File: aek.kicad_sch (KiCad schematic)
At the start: 242 parts, among them J1 Conn_01x04_MountingPin, SW1 SW_Push, U1 ATmega32U4-AU, U2 ATmega32U4-AU, Y1 16MHz

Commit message: updates
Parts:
- U2: value ATmega32U4-AU -> ATmega32U4-MU
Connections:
- net ROW1: now also U1.11 (PB3), U2.11 (PB3); no longer U1.18 (PD0), U2.18 (PD0)
- net ROW10: now also U1.9 (PB1), U2.9 (PB1); no longer U1.20 (PD2), U2.20 (PD2)
- net ROW2: now also U1.12 (PB7), U2.12 (PB7); no longer U1.9 (PB1), U2.9 (PB1)
- net ROW3: now also U1.19 (PD1), U2.19 (PD1); no longer U1.11 (PB3), U2.11 (PB3)
- net ROW7: now also U1.20 (PD2), U2.20 (PD2); no longer U1.12 (PB7), U2.12 (PB7)
- net ROW8: now also U1.18 (PD0), U2.18 (PD0); no longer U1.10 (PB2), U2.10 (PB2)
- net ROW9: now also U1.10 (PB2), U2.10 (PB2); no longer U1.19 (PD1), U2.19 (PD1)
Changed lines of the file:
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@@
     )
   )
-  (global_label "ROW2" (shape input) (at 87.63 62.23 0) (fields_autoplaced)
+  (global_label "ROW10" (shape input) (at 87.63 62.23 0) (fields_autoplaced)
     (effects (font (size 1.27 1.27)) (justify left))
-    (property "Intersheet References" "${INTERSHEET_REFS}" (id 0) (at 7.62 -41.91 0)
+    (property "Intersheet References" "${INTERSHEET_REFS}" (id 0) (at 7.62 -74.93 0)
       (effects (font (size 1.27 1.27)) hide)
     )
   )
-  (global_label "ROW8" (shape input) (at 87.63 64.77 0) (fields_autoplaced)
+  (global_label "ROW9" (shape input) (at 87.63 64.77 0) (fields_autoplaced)
     (effects (font (size 1.27 1.27)) (justify left))
-    (property "Intersheet References" "${INTERSHEET_REFS}" (id 0) (at 7.62 -41.91 0)
+    (property "Intersheet References" "${INTERSHEET_REFS}" (id 0) (at 7.62 -69.85 0)
       (effects (font (size 1.27 1.27)) hide)
     )
   )
-  (global_label "ROW3" (shape input) (at 87.63 67.31 0) (fields_autoplaced)
+  (global_label "ROW1" (shape input) (at 87.63 67.31 0) (fields_autoplaced)
     (effects (font (size 1.27 1.27)) (justify left))
-    (property "Intersheet References" "${INTERSHEET_REFS}" (id 0) (at 7.62 -41.91 0)
+    (property "Intersheet References" "${INTERSHEET_REFS}" (id 0) (at 7.62 -64.77 0)
       (effects (font (size 1.27 1.27)) hide)
     )
@@
     )
   )
-  (global_label "ROW7" (shape input) (at 87.63 77.47 0) (fields_autoplaced)
+  (global_label "ROW2" (shape input) (at 87.63 77.47 0) (fields_autoplaced)
     (effects (font (size 1.27 1.27)) (justify left))
-    (property "Intersheet References" "${INTERSHEET_REFS}" (id 0) (at 7.62 -41.91 0)
+    (property "Intersheet References" "${INTERSHEET_REFS}" (id 0) (at 7.62 -26.67 0)
       (effects (font (size 1.27 1.27)) hide)
     )
@@
     )
   )
-  (global_label "ROW1" (shape input) (at 87.63 90.17 0) (fields_autoplaced)
+  (global_label "ROW8" (shape input) (at 87.63 90.17 0) (fields_autoplaced)
     (effects (font (size 1.27 1.27)) (justify left))
-    (property "Intersheet References" "${INTERSHEET_REFS}" (id 0) (at 7.62 -41.91 0)
+    (property "Intersheet References" "${INTERSHEET_REFS}" (id 0) (at 7.62 -16.51 0)
       (effects (font (size 1.27 1.27)) hide)
     )
   )
-  (global_label "ROW9" (shape input) (at 87.63 92.71 0) (fields_autoplaced)
+  (global_label "ROW3" (shape input) (at 87.63 92.71 0) (fields_autoplaced)
     (effects (font (size 1.27 1.27)) (justify left))
-    (property "Intersheet References" "${INTERSHEET_REFS}" (id 0) (at 7.62 -41.91 0)
+    (property "Intersheet References" "${INTERSHEET_REFS}" (id 0) (at 7.62 -16.51 0)
       (effects (font (size 1.27 1.27)) hide)
     )
   )
-  (global_label "ROW10" (shape input) (at 87.63 95.25 0) (fields_autoplaced)
+  (global_label "ROW7" (shape input) (at 87.63 95.25 0) (fields_autoplaced)
     (effects (font (size 1.27 1.27)) (justify left))
-    (property "Intersheet References" "${INTERSHEET_REFS}" (id 0) (at 7.62 -41.91 0)
+    (property "Intersheet References" "${INTERSHEET_REFS}" (id 0) (at 7.62 -24.13 0)
       (effects (font (size 1.27 1.27)) hide)
     )
@@
     (in_bom yes) (on_board yes)
     (property "Reference" "U2" (id 0) (at 72.39 145.7706 0))
-    (property "Value" "ATmega32U4-AU" (id 1) (at 72.39 148.082 0))
+    (property "Value" "ATmega32U4-MU" (id 1) (at 72.39 148.082 0))
     (property "Footprint" "Package_DFN_QFN:QFN-44-1EP_7x7mm_P0.5mm_EP5.2x5.2mm" (id 2) (at 72.39 97.79 0)
       (effects (font (size 1.27 1.27) italic) hide)
@@
     )
     (path "/2ccdb65d-62ed-42d5-acea-df4cedf22149"
-      (reference "U2") (unit 1) (value "ATmega32U4-AU") (footprint "Package_DFN_QFN:QFN-44-1EP_7x7mm_P0.5mm_EP5.2x5.2mm")
+      (reference "U2") (unit 1) (value "ATmega32U4-MU") (footprint "Package_DFN_QFN:QFN-44-1EP_7x7mm_P0.5mm_EP5.2x5.2mm")
     )
     (path "/00000000-0000-0000-0000-0000612269b2"

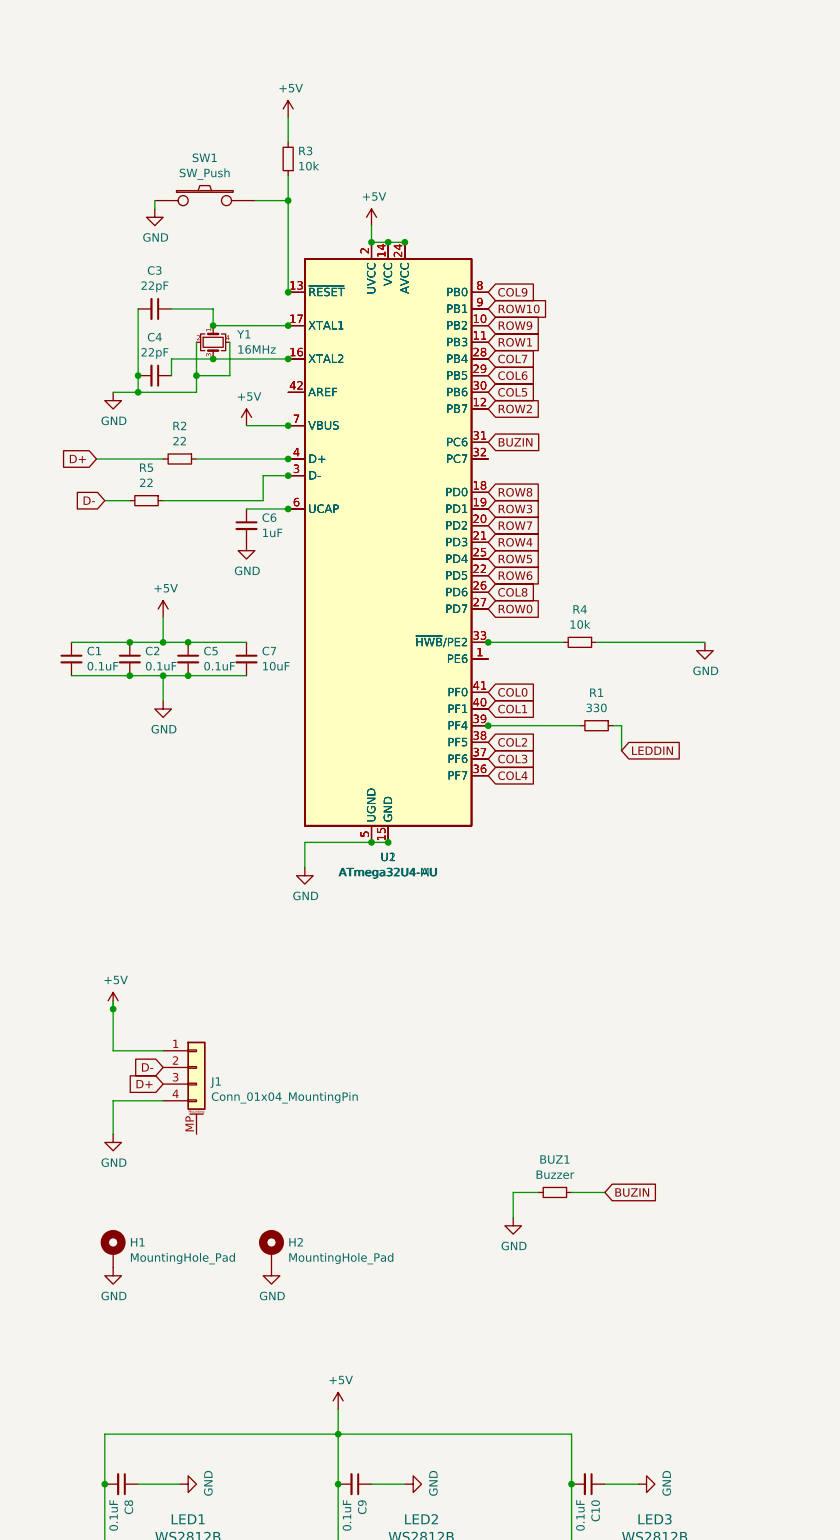
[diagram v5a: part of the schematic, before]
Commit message: continuous ground on F.Cu and custom footprint for merged au/mu atmega32u4
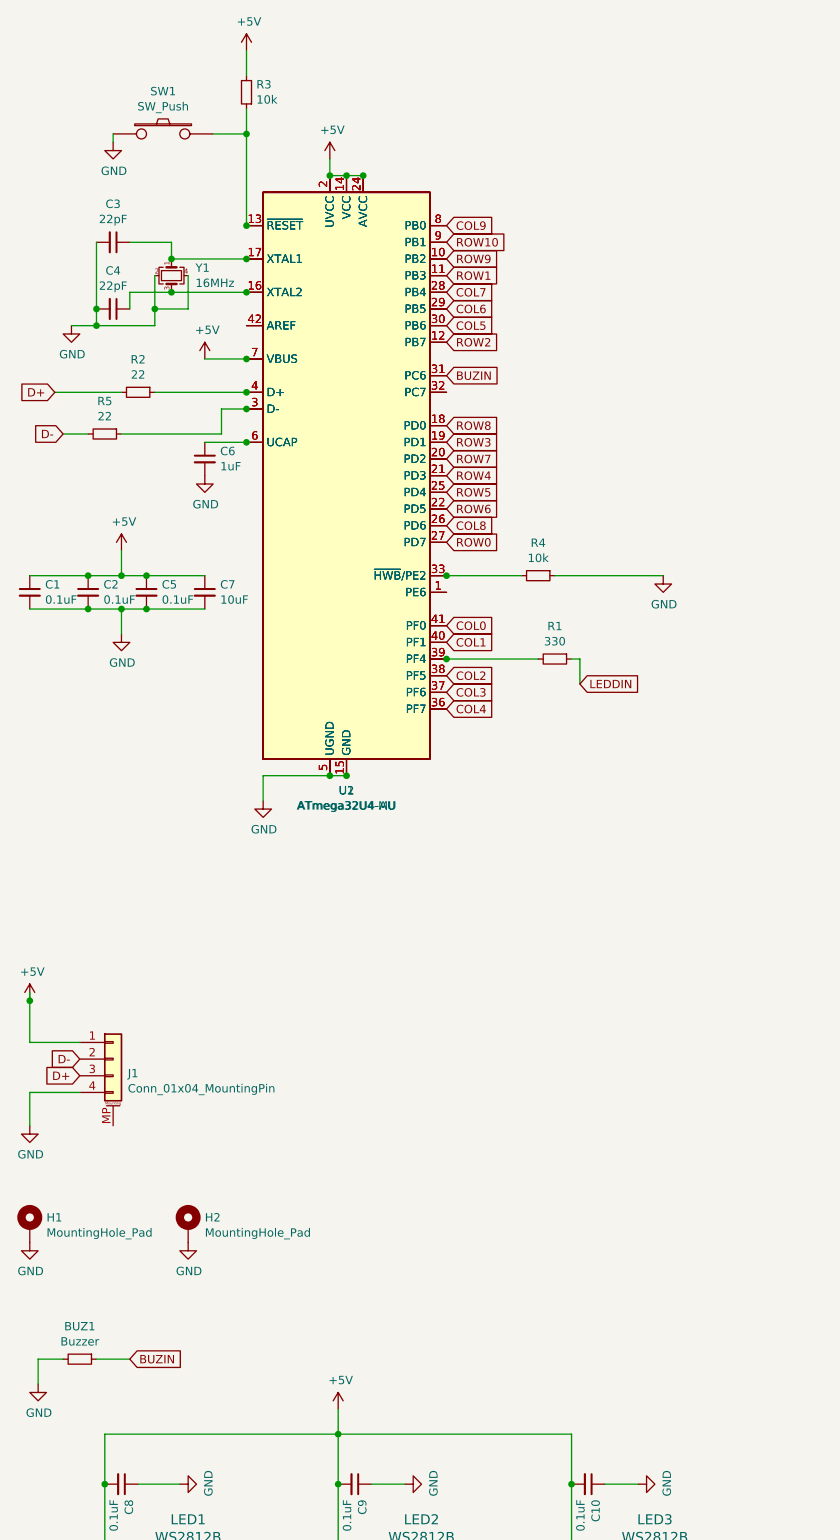
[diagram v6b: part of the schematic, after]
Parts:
- U2: symbol MCU_Microchip_ATmega:ATmega32U4-AU -> MCU_Microchip_ATmega:ATmega32U4-MU
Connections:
- net GND: now also U2.45 (GND)
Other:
- moved on the sheet: BUZ1, C1, C2, C3, C4, C5, C6, C7, H1, H2, J1, R1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

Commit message: cleanup
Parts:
- removed U1: ATmega32U4-AU, Package_QFP:TQFP-44_10x10mm_P0.8mm, symbol MCU_Microchip_ATmega:ATmega32U4-AU
- U1: renamed from U2; footprint Package_DFN_QFN:QFN-44-1EP_7x7mm_P0.5mm_EP5.2x5.2mm -> atmega32u4-au-and-mu:atmega32u4-mu-and-au
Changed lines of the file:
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@@
   (junction (at 39.37 59.69) (diameter 1.016) (color 0 0 0 0))
   (junction (at 50.8 35.56) (diameter 1.016) (color 0 0 0 0))
-  (junction (at 50.8 49.53) (diameter 1.016) (color 0 0 0 0))
-  (junction (at 50.8 54.61) (diameter 1.016) (color 0 0 0 0))
-  (junction (at 50.8 59.69) (diameter 1.016) (color 0 0 0 0))
-  (junction (at 50.8 69.85) (diameter 1.016) (color 0 0 0 0))
-  (junction (at 50.8 74.93) (diameter 1.016) (color 0 0 0 0))
-  (junction (at 50.8 77.47) (diameter 1.016) (color 0 0 0 0))
-  (junction (at 50.8 82.55) (diameter 1.016) (color 0 0 0 0))
   (junction (at 63.5 41.91) (diameter 1.016) (color 0 0 0 0))
   (junction (at 63.5 133.35) (diameter 1.016) (color 0 0 0 0))
@@
   (junction (at 64.77 241.3) (diameter 1.016) (color 0 0 0 0))
   (junction (at 66.04 41.91) (diameter 1.016) (color 0 0 0 0))
-  (junction (at 66.04 133.35) (diameter 1.016) (color 0 0 0 0))
-  (junction (at 68.58 41.91) (diameter 1.016) (color 0 0 0 0))
-  (junction (at 81.28 102.87) (diameter 1.016) (color 0 0 0 0))
-  (junction (at 81.28 115.57) (diameter 1.016) (color 0 0 0 0))
   (junction (at 100.33 241.3) (diameter 1.016) (color 0 0 0 0))
   (junction (at 157.48 55.88) (diameter 1.016) (color 0 0 0 0))
@@
     (pin "4")
   )
-  (symbol (lib_id "MCU_Microchip_ATmega:ATmega32U4-AU") (at 66.04 87.63 0) (unit 1)
-    (in_bom yes) (on_board yes)
-    (property "Reference" "U1" (id 0) (at 66.04 135.6106 0))
-    (property "Value" "ATmega32U4-AU" (id 1) (at 66.04 137.922 0))
-    (property "Footprint" "Package_QFP:TQFP-44_10x10mm_P0.8mm" (id 2) (at 66.04 87.63 0)
-      (effects (font (size 1.27 1.27) italic) hide)
-    )
-    (property "Datasheet" "http://ww1.microchip.com/downloads/en/DeviceDoc/Atmel-7766-8-bit-AVR-ATmega16U4-32U4_Datasheet.pdf" (id 3) (at 66.04 87.63 0)
-      (effects (font (size 1.27 1.27)) hide)
-    )
-    (pin "1")
-    (pin "10")
-    (pin "11")
-    (pin "12")
-    (pin "13")
-    (pin "14")
-    (pin "15")
-    (pin "16")
-    (pin "17")
-    (pin "18")
-    (pin "19")
-    (pin "2")
-    (pin "20")
-    (pin "21")
-    (pin "22")
-    (pin "23")
-    (pin "24")
-    (pin "25")
-    (pin "26")
-    (pin "27")
-    (pin "28")
-    (pin "29")
-    (pin "3")
-    (pin "30")
-    (pin "31")
-    (pin "32")
-    (pin "33")
-    (pin "34")
-    (pin "35")
-    (pin "36")
-    (pin "37")
-    (pin "38")
-    (pin "39")
-    (pin "4")
-    (pin "40")
-    (pin "41")
-    (pin "42")
-    (pin "43")
-    (pin "44")
-    (pin "5")
-    (pin "6")
-    (pin "7")
-    (pin "8")
-    (pin "9")
-  )
   (symbol (lib_id "MCU_Microchip_ATmega:ATmega32U4-MU") (at 66.04 87.63 0) (unit 1)
     (in_bom yes) (on_board yes)
-    (property "Reference" "U2" (id 0) (at 66.04 135.6106 0))
+    (property "Reference" "U1" (id 0) (at 66.04 135.6106 0))
     (property "Value" "ATmega32U4-MU" (id 1) (at 66.04 137.922 0))
-    (property "Footprint" "Package_DFN_QFN:QFN-44-1EP_7x7mm_P0.5mm_EP5.2x5.2mm" (id 2) (at 66.04 87.63 0)
+    (property "Footprint" "atmega32u4-au-and-mu:atmega32u4-mu-and-au" (id 2) (at 66.04 87.63 0)
       (effects (font (size 1.27 1.27) italic) hide)
     )
@@
       (reference "SW_Z1") (unit 1) (value "MX-NoLED") (footprint "MX_Alps_Hybrid:MX-1U-NoLED")
     )
-    (path "/00000000-0000-0000-0000-0000611ebb71"
-      (reference "U1") (unit 1) (value "ATmega32U4-AU") (footprint "Package_QFP:TQFP-44_10x10mm_P0.8mm")
-    )
     (path "/2ccdb65d-62ed-42d5-acea-df4cedf22149"
-      (reference "U2") (unit 1) (value "ATmega32U4-MU") (footprint "Package_DFN_QFN:QFN-44-1EP_7x7mm_P0.5mm_EP5.2x5.2mm")
+      (reference "U1") (unit 1) (value "ATmega32U4-MU") (footprint "atmega32u4-au-and-mu:atmega32u4-mu-and-au")
     )
     (path "/00000000-0000-0000-0000-0000612269b2"

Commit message: bug fixes
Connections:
- net +5V: now also J1.4 (Pin_4); no longer J1.1 (Pin_1)
- net D+: now also J1.2 (Pin_2); no longer J1.3 (Pin_3)
- net D-: now also J1.3 (Pin_3); no longer J1.2 (Pin_2)
- net GND: now also J1.1 (Pin_1); no longer J1.4 (Pin_4)
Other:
- moved on the sheet: J1
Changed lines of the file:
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@@
 (kicad_sch (version 20210621) (generator eeschema)
   (paper "User" 359.994 359.994)
-  (junction (at 17.78 167.64) (diameter 1.016) (color 0 0 0 0))
   (junction (at 26.67 102.87) (diameter 1.016) (color 0 0 0 0))
   (junction (at 26.67 107.95) (diameter 1.016) (color 0 0 0 0))
@@
   (junction (at 39.37 59.69) (diameter 1.016) (color 0 0 0 0))
   (junction (at 50.8 35.56) (diameter 1.016) (color 0 0 0 0))
+  (junction (at 53.34 170.18) (diameter 1.016) (color 0 0 0 0))
   (junction (at 63.5 41.91) (diameter 1.016) (color 0 0 0 0))
   (junction (at 63.5 133.35) (diameter 1.016) (color 0 0 0 0))
@@
     (stroke (width 0) (type solid) (color 0 0 0 0))
   )
-  (wire (pts (xy 17.78 166.37) (xy 17.78 167.64))
-    (stroke (width 0) (type solid) (color 0 0 0 0))
-  )
-  (wire (pts (xy 17.78 167.64) (xy 17.78 173.99))
-    (stroke (width 0) (type solid) (color 0 0 0 0))
-  )
-  (wire (pts (xy 17.78 181.61) (xy 17.78 186.69))
-    (stroke (width 0) (type solid) (color 0 0 0 0))
-  )
   (wire (pts (xy 19.05 222.25) (xy 19.05 226.06))
     (stroke (width 0) (type solid) (color 0 0 0 0))
@@
     (stroke (width 0) (type solid) (color 0 0 0 0))
   )
-  (wire (pts (xy 25.4 173.99) (xy 17.78 173.99))
-    (stroke (width 0) (type solid) (color 0 0 0 0))
-  )
-  (wire (pts (xy 25.4 181.61) (xy 17.78 181.61))
-    (stroke (width 0) (type solid) (color 0 0 0 0))
-  )
   (wire (pts (xy 26.67 102.87) (xy 31.75 102.87))
     (stroke (width 0) (type solid) (color 0 0 0 0))
@@
     (stroke (width 0) (type solid) (color 0 0 0 0))
   )
+  (wire (pts (xy 45.72 175.26) (xy 53.34 175.26))
+    (stroke (width 0) (type solid) (color 0 0 0 0))
+  )
   (wire (pts (xy 46.99 77.47) (xy 50.8 77.47))
     (stroke (width 0) (type solid) (color 0 0 0 0))
@@
     (stroke (width 0) (type solid) (color 0 0 0 0))
   )
+  (wire (pts (xy 53.34 168.91) (xy 53.34 170.18))
+    (stroke (width 0) (type solid) (color 0 0 0 0))
+  )
+  (wire (pts (xy 53.34 170.18) (xy 53.34 175.26))
+    (stroke (width 0) (type solid) (color 0 0 0 0))
+  )
+  (wire (pts (xy 53.34 182.88) (xy 45.72 182.88))
+    (stroke (width 0) (type solid) (color 0 0 0 0))
+  )
+  (wire (pts (xy 53.34 182.88) (xy 53.34 189.23))
+    (stroke (width 0) (type solid) (color 0 0 0 0))
+  )
   (wire (pts (xy 54.61 259.08) (xy 54.61 254))
     (stroke (width 0) (type solid) (color 0 0 0 0))
@@
     )
   )
-  (global_label "D-" (shape input) (at 25.4 176.53 180) (fields_autoplaced)
-    (effects (font (size 1.27 1.27)) (justify right))
-    (property "Intersheet References" "${INTERSHEET_REFS}" (id 0) (at -12.7 -40.64 0)
-      (effects (font (size 1.27 1.27)) hide)
+  (global_label "BUZIN" (shape input) (at 33.02 222.25 0) (fields_autoplaced)
+    (effects (font (size 1.27 1.27)) (justify left))
+    (property "Intersheet References" "${INTERSHEET_REFS}" (id 0) (at 41.0386 222.1706 0)
+      (effects (font (size 1.27 1.27)) (justify left) hide)
     )
   )
-  (global_label "D+" (shape input) (at 25.4 179.07 180) (fields_autoplaced)
-    (effects (font (size 1.27 1.27)) (justify right))
-    (property "Intersheet References" "${INTERSHEET_REFS}" (id 0) (at -12.7 -40.64 0)
+  (global_label "D-" (shape input) (at 45.72 177.8 0) (fields_autoplaced)
+    (effects (font (size 1.27 1.27)) (justify left))
+    (property "Intersheet References" "${INTERSHEET_REFS}" (id 0) (at 83.82 394.97 0)
       (effects (font (size 1.27 1.27)) hide)
     )
   )
-  (global_label "BUZIN" (shape input) (at 33.02 222.25 0) (fields_autoplaced)
+  (global_label "D+" (shape input) (at 45.72 180.34 0) (fields_autoplaced)
     (effects (font (size 1.27 1.27)) (justify left))
-    (property "Intersheet References" "${INTERSHEET_REFS}" (id 0) (at 41.0386 222.1706 0)
-      (effects (font (size 1.27 1.27)) (justify left) hide)
+    (property "Intersheet References" "${INTERSHEET_REFS}" (id 0) (at 83.82 400.05 0)
+      (effects (font (size 1.27 1.27)) hide)
     )
   )
@@
     )
   )
-  (symbol (lib_id "power:+5V") (at 17.78 167.64 0) (unit 1)
-    (in_bom yes) (on_board yes)
-    (property "Reference" "#PWR0111" (id 0) (at 17.78 171.45 0)
-      (effects (font (size 1.27 1.27)) hide)
-    )
-    (property "Value" "+5V" (id 1) (at 18.161 163.2458 0))
-    (property "Footprint" "" (id 2) (at 17.78 167.64 0)
-      (effects (font (size 1.27 1.27)) hide)
-    )
-    (property "Datasheet" "" (id 3) (at 17.78 167.64 0)
-      (effects (font (size 1.27 1.27)) hide)
-    )
-    (pin "1")
-  )
   (symbol (lib_id "power:+5V") (at 31.75 99.06 0) (unit 1)
     (in_bom yes) (on_board yes)
@@
     (pin "1")
   )
+  (symbol (lib_id "power:+5V") (at 53.34 170.18 0) (unit 1)
+    (in_bom yes) (on_board yes)
+    (property "Reference" "#PWR0111" (id 0) (at 53.34 173.99 0)
+      (effects (font (size 1.27 1.27)) hide)
+    )
+    (property "Value" "+5V" (id 1) (at 53.721 165.7858 0))
+    (property "Footprint" "" (id 2) (at 53.34 170.18 0)
+      (effects (font (size 1.27 1.27)) hide)
+    )
+    (property "Datasheet" "" (id 3) (at 53.34 170.18 0)
+      (effects (font (size 1.27 1.27)) hide)
+    )
+    (pin "1")
+  )
   (symbol (lib_id "power:+5V") (at 63.5 39.37 0) (unit 1)
     (in_bom yes) (on_board yes)
@@
     (pin "1")
   )
-  (symbol (lib_id "power:GND") (at 17.78 186.69 0) (unit 1)
-    (in_bom yes) (on_board yes)
-    (property "Reference" "#PWR0112" (id 0) (at 17.78 193.04 0)
-      (effects (font (size 1.27 1.27)) hide)
-    )
-    (property "Value" "GND" (id 1) (at 17.907 191.0842 0))
-    (property "Footprint" "" (id 2) (at 17.78 186.69 0)
-      (effects (font (size 1.27 1.27)) hide)
-    )
-    (property "Datasheet" "" (id 3) (at 17.78 186.69 0)
-      (effects (font (size 1.27 1.27)) hide)
-    )
-    (pin "1")
-  )
   (symbol (lib_id "power:GND") (at 17.78 204.47 0) (unit 1)
     (in_bom yes) (on_board yes)
@@
     (pin "1")
   )
+  (symbol (lib_id "power:GND") (at 53.34 189.23 0) (unit 1)
+    (in_bom yes) (on_board yes)
+    (property "Reference" "#PWR0112" (id 0) (at 53.34 195.58 0)
+      (effects (font (size 1.27 1.27)) hide)
+    )
+    (property "Value" "GND" (id 1) (at 53.467 193.6242 0))
+    (property "Footprint" "" (id 2) (at 53.34 189.23 0)
+      (effects (font (size 1.27 1.27)) hide)
+    )
+    (property "Datasheet" "" (id 3) (at 53.34 189.23 0)
+      (effects (font (size 1.27 1.27)) hide)
+    )
+    (pin "1")
+  )
   (symbol (lib_id "power:GND") (at 54.61 270.51 0) (unit 1)
     (in_bom yes) (on_board yes)
@@
     (pin "2")
   )
-  (symbol (lib_id "Connector_Generic_MountingPin:Conn_01x04_MountingPin") (at 30.48 176.53 0) (unit 1)
+  (symbol (lib_id "Connector_Generic_MountingPin:Conn_01x04_MountingPin") (at 40.64 180.34 180) (unit 1)
     (in_bom yes) (on_board yes)
-    (property "Reference" "J1" (id 0) (at 32.7152 178.7144 0)
+    (property "Reference" "J1" (id 0) (at 38.4048 178.1556 0)
       (effects (font (size 1.27 1.27)) (justify left))
     )
-    (property "Value" "Conn_01x04_MountingPin" (id 1) (at 32.7152 181.0258 0)
+    (property "Value" "Conn_01x04_MountingPin" (id 1) (at 73.9648 178.3842 90)
       (effects (font (size 1.27 1.27)) (justify left))
     )
-    (property "Footprint" "Connector_JST:JST_SH_SM04B-SRSS-TB_1x04-1MP_P1.00mm_Horizontal" (id 2) (at 30.48 176.53 0)
+    (property "Footprint" "Connector_JST:JST_SH_SM04B-SRSS-TB_1x04-1MP_P1.00mm_Horizontal" (id 2) (at 40.64 180.34 0)
       (effects (font (size 1.27 1.27)) hide)
     )
-    (property "Datasheet" "~" (id 3) (at 30.48 176.53 0)
+    (property "Datasheet" "~" (id 3) (at 40.64 180.34 0)
       (effects (font (size 1.27 1.27)) hide)
     )
